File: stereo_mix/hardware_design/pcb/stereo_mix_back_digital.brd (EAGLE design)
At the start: 70 x 100 mm, 236 parts, among them IC1 LD117AS50TR, J1 WQP-PJ301M-12_JACK, J10 WQP-PJ301M-12_JACK, J11 WQP-PJ301M-12_JACK, J12 WQP-PJ301M-12_JACK, J13 WQP-PJ301M-12_JACK, J14 WQP-PJ301M-12_JACK, J15 WQP-PJ301M-12_JACK, J16 WQP-PJ301M-12_JACK, J17 WQP-PJ301M-12_JACK, J18 WQP-PJ301M-12_JACK, J2 WQP-PJ301M-12_JACK, J3 WQP-PJ301M-12_JACK, J4 WQP-PJ301M-12_JACK, J5 WQP-PJ301M-12_JACK, J6 WQP-PJ301M-12_JACK, J7 WQP-PJ301M-12_JACK, J8 WQP-PJ301M-12_JACK, J9 WQP-PJ301M-12_JACK, U1 TL072AD, U10 TL072AD, U11 MCP6002E/SN, U12 MCP6002E/SN, U13 MCP6002E/SN, U14 MCP6002E/SN, U15 MCP4922E/SL, U16 MCP4922E/SL, U17 TL072AD, U18 TL072AD, U19 MCP4822E-SN, U2 MCP6002E/SN, U20 MCP4822E-SN, U21 TL072AD, U22 TL072AD, U23 ATMEGA328P-AU, U24 MCP4822E-SN, U25 MCP4822E-SN, U26 TL072AD, U27 TL072AD, U28 TL072AD, U3 MCP6002E/SN, U4 MCP6002E/SN, U5 MCP6002E/SN, U6 MCP4922E/SL, U7 MCP4922E/SL, U8 TL072AD, U9 TL072AD

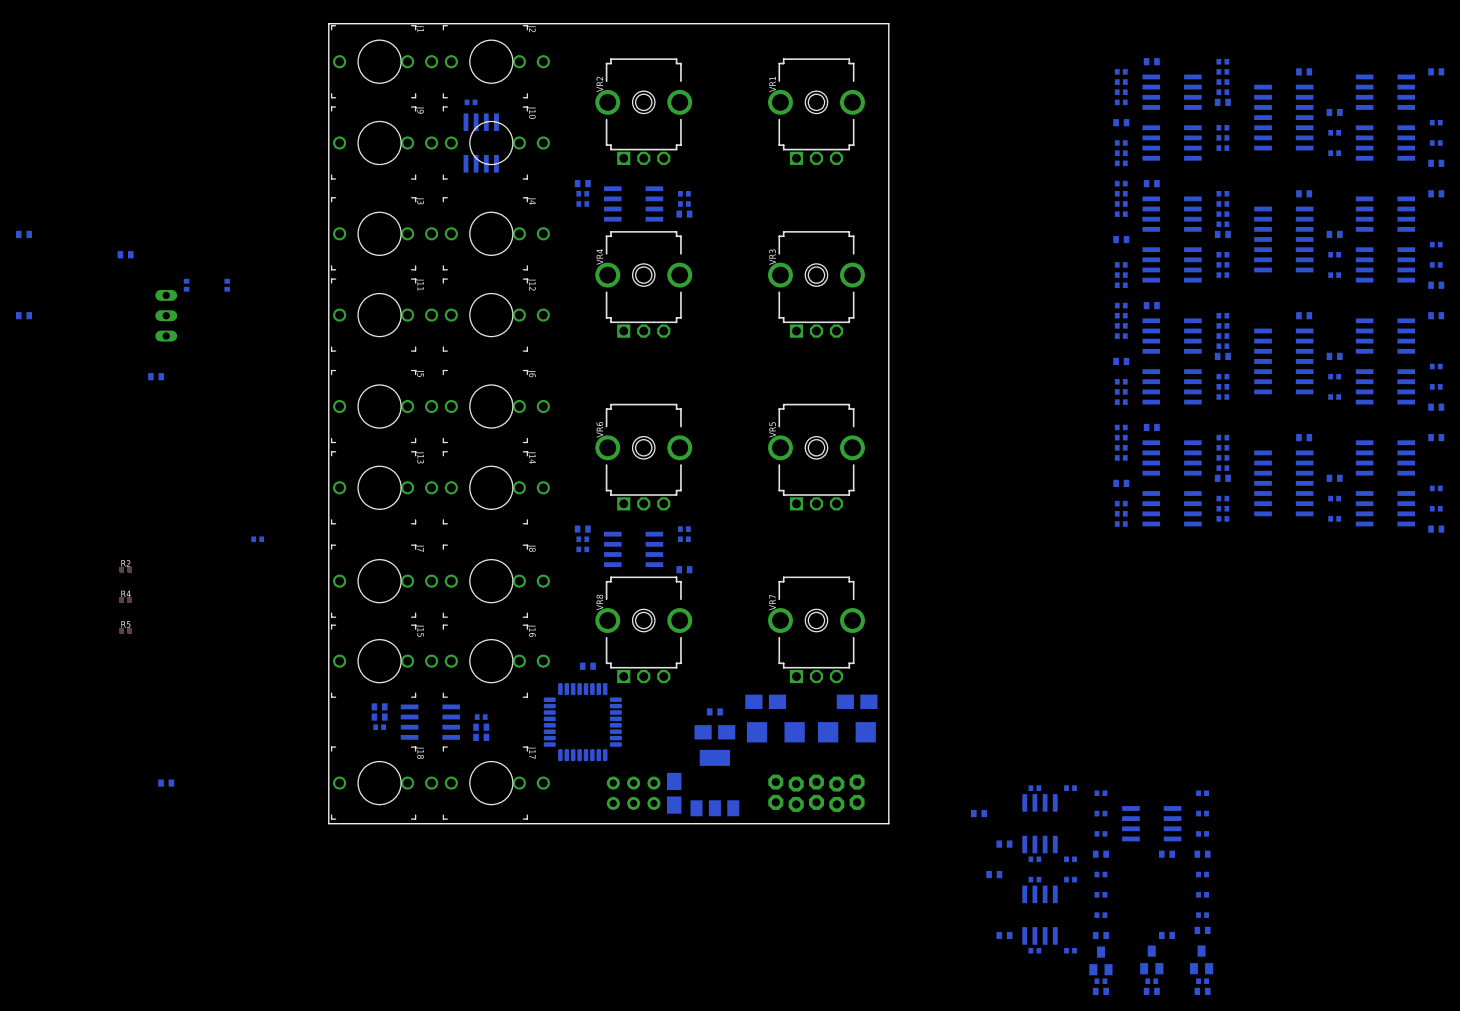
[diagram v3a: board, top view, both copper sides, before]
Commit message: Add new hardware revision of stereo mix
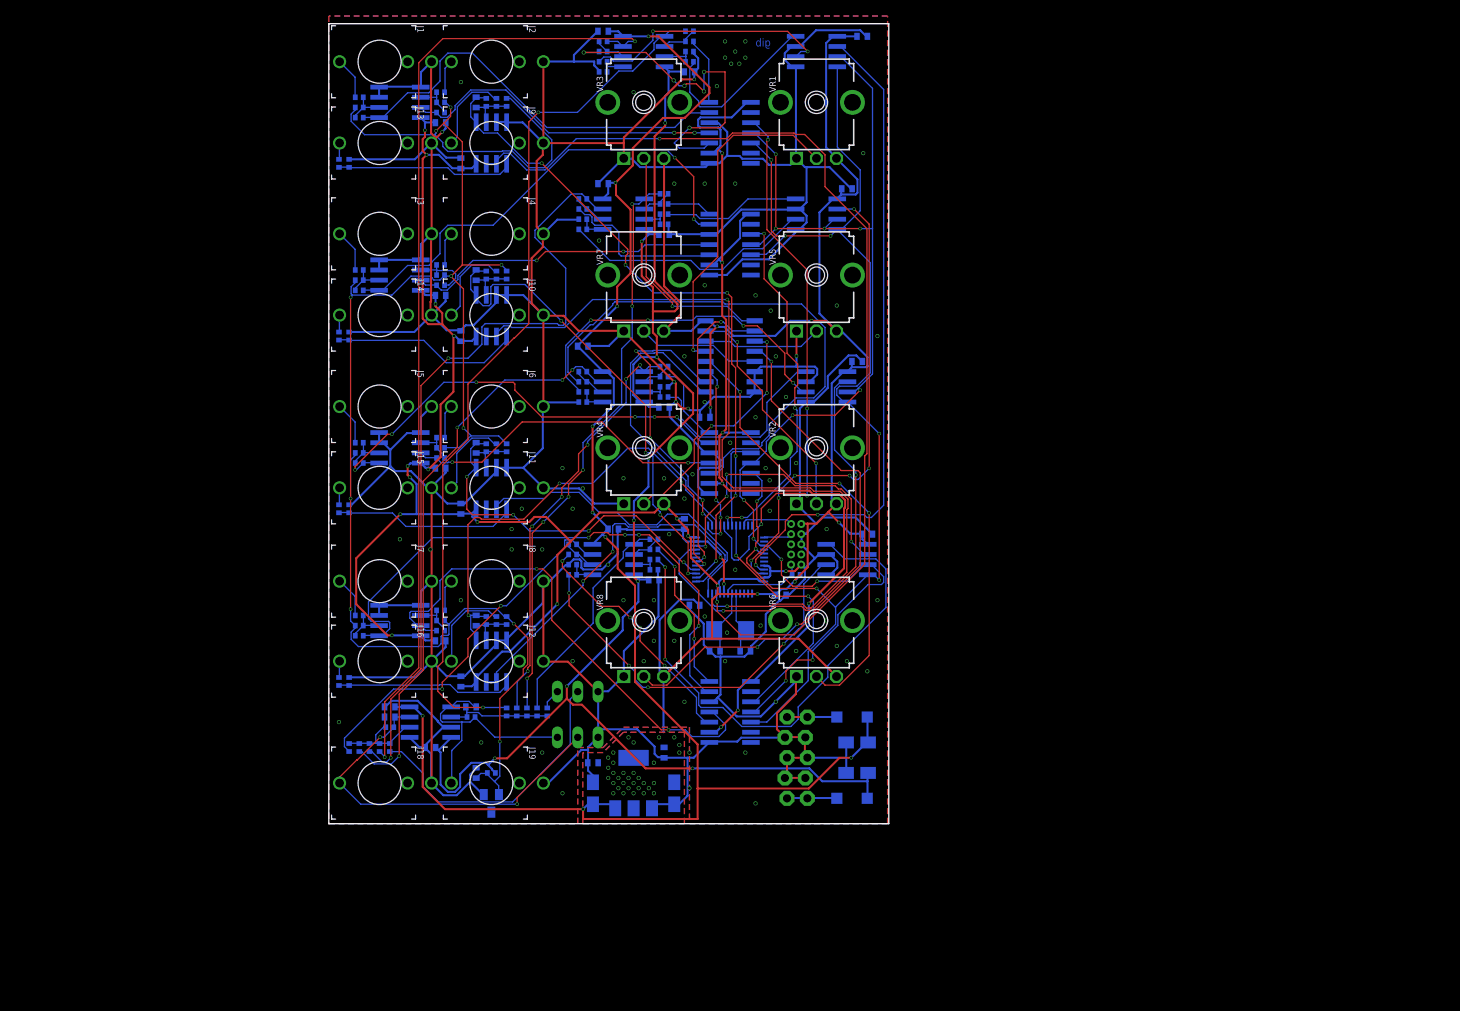
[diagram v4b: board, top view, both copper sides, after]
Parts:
- removed C45, C46, C47, C50, C51, C52, C53, C54, C58, C61, C62, C63: 100nF, jhbruhn-cr:C0402
- removed C48, C49: 6.8pF, jhbruhn-cr:C0402
- removed C55: EURO_POWER_LOCKFAT-LOCK, MusicThingModular:EURO_PWR_HEADER_LOCK
- removed C56, C57, C59, C60: 47uF, rcl:A/3216-18W
- removed D4, D5: LM4040AIM3-10.0, jhbruhn-ref:SOT23
- removed ISP1: AVRISP-6, adafruit:AVRISP
- removed JP3: (no value), jumper:JP2
- removed R100, R105, R106, R107, R108, R110, R111, R112, R113, R114, R91, R92, R97, R98, R99: 100k, jhbruhn-cr:R0402
- removed R101, R102, R103, R104, R93, R94, R95, R96: 43k, jhbruhn-cr:R0402
- removed R109: 10k, jhbruhn-cr:R0402
- removed R122, R123, R124: 470R, jhbruhn-cr:R0402
- removed U23: ATMEGA328P-AU, jhbruhn-mcu:TQFP-32
- removed U24, U25: MCP4822E-SN, jhbruhn-dac:SOIC8
- removed U26, U27, U28: TL072AD, jhbruhn-opamp:SOIC8
- added IC2: AMS1117-3.3, jhbruhn-ic:SOT223
- added J19: WQP-PJ301M-12_JACK, jhbruhn-physical:WQP-PJ301M-12_JACK
- added JP1, JP2: (no value), jumper:JP2
- added R44: 15k, jhbruhn-cr:R0402
- added R46, R49, R50: 47k, jhbruhn-cr:R0402
- added R6: 100k, jhbruhn-cr:R0402
- added X1: 8MHz, jhbruhn-cdr:NX5032
- C11, C12: value 4.7nF -> 100nF
- C21, C22: value 100nF -> 4.7nF
- C26, C27: value 100nF -> 22pF
- C32, C33: value 100nF -> 6.8pF
- C36: value 100nF -> EURO_POWER_LOCKFAT-LOCK; device jhbruhn-cr:C0402 -> MusicThingModular:EURO_PWR_HEADER_LOCK
- C37, C38, C39, C41: value 100nF -> 10uF; device jhbruhn-cr:C0402 -> jhbruhn-cdr:A/3216-18R
- D1, D2: value 1N4001 -> 1N4148W; device adafruit:SMADIODE -> jhbruhn-cdr:SOD123
- D3: value LM4040AIM3-5.0 -> LM4040AIM3-10.0
- IC1: value LD117AS50TR -> 4051D; device v-reg:SOT223 -> jhbruhn-ic:SO16
- J17: value WQP-PJ301M-12_JACK -> CORTEX_DEBUG_PTH; device jhbruhn-physical:WQP-PJ301M-12_JACK -> jhbruhn-physical:2X5-PTH-1.27MM
- R1, R3, R33, R37, R39, R5, R7: value 100k -> 91k
- R10, R11, R12, R41, R42, R43, R9: value 100k -> 15k
- R13, R14, R15, R16, R45, R47, R48, R51, R52: value 100k -> 47k
- R17, R18, R19, R20: value 24k -> 47k
- R21: value 200k -> 100k
- R23: value 200k -> 300k
- R25, R28, R57, R58, R59, R60: value 100k -> 300k
- R26: value 51k -> 300k
- R27: value 51k -> 100k
- R30, R31, R34, R66, R68, R82, R83: value 24k -> 100k
- R35: value 24k -> 91k
- R65, R67, R78, R79: value 24k -> 200k
- R73, R74: value 51k -> 33k
- R75, R76: value 100k -> 33k
- R77, R80: value 100k -> 200k
- R85: value 100k -> 10k
- R90: value 100k -> 470R
- U1, U10, U9: value TL072AD -> MCP4822E-SN; device jhbruhn-opamp:SOIC8 -> jhbruhn-dac:SOIC8
- U11, U12, U3, U4: value MCP6002E/SN -> MCP6002T-I/SN
- U13, U14, U5: value MCP6002E/SN -> MCP4922E/SL; device jhbruhn-opamp:SOIC8 -> jhbruhn-dac:SO-14
- U15, U16, U7: value MCP4922E/SL -> TL072CD; device jhbruhn-dac:SO-14 -> jhbruhn-opamp:SOIC8
- U17, U18: value TL072AD -> MCP6002T-I/SN
- U19, U20: value MCP4822E-SN -> MCP6002T-I/SN; device jhbruhn-dac:SOIC8 -> jhbruhn-opamp:SOIC8
- U2: value MCP6002E/SN -> MCP4822E-SN; device jhbruhn-opamp:SOIC8 -> jhbruhn-dac:SOIC8
- U21: value TL072AD -> STM32F030C8T6; device jhbruhn-opamp:SOIC8 -> jhbruhn-mcu:LQFP48
- U22, U8: value TL072AD -> TL072CD
- moved C35 153.0 mm to (7.62, 14.6), turned to 0 degrees
- moved C40 142.2 mm to (18.4, 6.35), turned to 90 degrees
- moved R30 133.5 mm to (6.35, 9.53), turned to 90 degrees
- moved U22 132.4 mm to (12.7, 12.7)
- moved R38 127.6 mm to (3.81, 26.0)
- moved U20 125.0 mm to (20.3, 20.3), turned to 180 degrees
- moved R32 124.7 mm to (5.08, 9.53), turned to 90 degrees
- moved R23 123.4 mm to (45.1, 99.1)
- moved R24 123.4 mm to (45.1, 96.5), turned to 180 degrees
- moved C39 123.1 mm to (33.0, 3.81), turned to 90 degrees
- moved U19 122.2 mm to (20.3, 41.9), turned to 180 degrees
- moved C19 122.2 mm to (18.4, 90.2), turned to 90 degrees
- moved R73 119.4 mm to (19.7, 90.2), turned to 90 degrees
- moved R29 119.2 mm to (22.2, 14.0), turned to 270 degrees
- moved R21 118.1 mm to (34.3, 94.0)
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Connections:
- removed net 1_PAN_CV_IN: J10.P$1_TIP, R114.1
- removed net 1_VOLUME_CV: J9.P$1_TIP, R25.2
- removed net N$12: U1.3, VR2.2
- removed net N$13: R22.1, R7.2, U1.1
- removed net N$18: R1.2, R7.1, U1.2
- removed net N$43: U1.5, VR4.2
- removed net N$45: U10.5, VR8.2
- removed net N$56: R24.1, R8.2, U1.7
- removed net N$57: R3.2, R8.1, U1.6
- removed net N$58: C34.1, U23.20
- removed net N$60: R53.2, R70.1, U10.1
- removed net N$61: R43.2, R53.1, U10.2
- removed net N$64: R54.2, R72.1, U10.7
- removed net N$65: R45.2, R54.1, U10.6
- removed net N$74: R93.2, R97.1, U21.2
- removed net N$77: R100.1, R96.2, U22.6
- removed net N$78: R101.2, R105.1, U26.2
- removed net N$79: R102.2, R106.1, U26.6
- removed net N$80: R103.2, R107.1, U27.2
- removed net N$81: R104.2, R108.1, U27.6
- removed net N$83: U10.3, VR6.2
- removed net REF_10: C61.1, D4.1, R123.1
- removed net REF_5: C58.1, D3.1, R1.1, R122.1, R3.1, R43.1, R45.1, VR2.3, VR4.3, VR6.3, VR8.3
- removed net RESET: ISP1.5, R109.1, U23.29
- new net +3V3: C10.1, C11.1, C12.1, C13.1, C14.1, C15.1, C16.1, C17.1, C18.1, C23.1, C24.1, C25.1, C28.1, C29.1, C30.1, C31.1, C41.+, C42.1, C9.1, IC1.16, IC2.4, J17.1, R85.2, U1.1, U10.1, U11.8, U12.8, U17.8, U18.8, U19.8, U2.1, U20.8, U21.1, U21.24, U21.48, U21.9, U3.8, U4.8, U9.1, VR1.3, VR2.3, VR3.3, VR4.3, VR5.3, VR6.3, VR7.3, VR8.3
- new net MUX_ADDR_0: IC1.11, U21.25
- new net MUX_ADDR_1: IC1.10, U21.26
- new net MUX_ADDR_2: IC1.9, U21.27
- new net N$84: J9.P$1_TIP, R66.1
- new net N$89: J13.P$1_TIP, R77.2
- new net NRST: J17.10, R85.1, U21.7
- new net PAN_1_POT: IC1.1, VR3.2
- new net PAN_2_POT: IC1.5, VR7.2
- new net PAN_3_POT: IC1.2, VR4.2
- new net PAN_4_POT: IC1.4, VR8.2
- new net POT_MUX: IC1.3, U21.18
- new net SWDCLK: J17.4, U21.37
- new net SWDIO: J17.2, U21.34
- new net VOL_1_POT: IC1.13, VR1.2
- new net VOL_2_POT: IC1.14, VR5.2
- new net VOL_3_POT: IC1.15, VR2.2
- new net VOL_4_POT: IC1.12, VR6.2
- net +12V: now also C35.1, C37.+, C39.+, IC2.3, U15.8, U16.8, U7.8; no longer C13.1, C41.1, C42.1, C45.1, C46.1, C52.1, C53.1, C54.1, C56.+, C59.+, C9.1, IC1.3, R122.2, R123.2, U1.8, U10.8, U17.8, U18.8, U21.8, U26.8, U27.8, U28.8, U9.8
- net +5V: now also U13.1, U13.9, U14.1, U14.9, U5.1, U5.9; no longer C15.1, C16.1, C17.1, C18.1, C21.1, C22.1, C23.1, C24.1, C25.1, C26.1, C27.1, C28.1, C29.1, C30.1, C31.1, C32.1, C33.1, C35.1, C36.1, C60.+, C62.1, IC1.4, ISP1.2, R109.2, U11.8, U12.8, U13.8, U14.8, U15.1, U15.9, U16.1, U16.9, U19.1, U2.8, U20.1, U23.18, U23.4, U23.6, U24.1, U25.1, U3.8, U4.8, U5.8, U7.1, U7.9
- net -12V: now also C34.2, C38.-, R90.2, U15.4, U16.4, U7.4; no longer C10.2, C14.2, C37.2, C38.2, C39.2, C40.2, C47.2, C50.2, C51.2, C57.-, R124.2, U1.4, U10.4, U17.4, U18.4, U21.4, U26.4, U27.4, U28.4, U9.4
- net 1_IN_L: now also R2.1; no longer R10.1
- net 1_IN_R: now also R4.1; no longer R12.1
- net 2_IN_L: now also R6.1; no longer R14.1
- net 2_IN_R: now also R8.1; no longer R16.1
- net 2_PAN_CV_IN: now also J10.P$1_TIP, R68.1; no longer J12.P$1_TIP, R2.1
- net 2_VOLUME_CV: now also J14.P$1_TIP, R78.2; no longer J11.P$1_TIP, R37.2
- net 3_IN_L: now also R34.1; no longer R56.1
- net 3_IN_R: now also R36.1; no longer R58.1
- net 3_PAN_CV_IN: now also J11.P$1_TIP, R70.1; no longer J14.P$1_TIP, R4.1
- net 3_VOLUME_CV: now also J15.P$1_TIP, R79.2; no longer J13.P$1_TIP, R63.2
- net 4_IN_L: now also R38.1; no longer R60.1
- net 4_IN_R: now also R40.1; no longer R62.1
- net 4_PAN_CV_IN: now also J12.P$1_TIP, R72.1; no longer J16.P$1_TIP, R5.1
- net 4_VOLUME_CV: now also J16.P$1_TIP, R80.2; no longer J15.P$1_TIP, R75.2
- net AREF_-10: now also C40.1, D3.2, R1.1, R3.1, R33.1, R35.1, R37.1, R39.1, R5.1, R65.1, R67.1, R7.1, R90.1; no longer C63.1, D5.2, R11.1, R124.1, R13.1, R15.1, R21.1, R23.1, R55.1, R57.1, R59.1, R61.1, R9.1
- net AUX_IN_L: now also JP1.1, R86.1; no longer JP3.1, R110.1
- net AUX_IN_R: now also JP1.2, R87.1; no longer JP3.2, R111.1
- net BIAS_DAC1_L: now also R16.1, U1.8; no longer R29.1, R97.2, U21.1
- net BIAS_DAC1_R: now also R15.1, U1.6; no longer R32.1, R98.2, U21.7
- net BIAS_DAC2_L: now also R20.1, U2.8; no longer R33.1, R99.2, U22.1
- net BIAS_DAC2_R: now also R19.1, U2.6; no longer R100.2, R36.1, U22.7
- net BIAS_DAC3_L: now also R51.1, U9.8; no longer R105.2, R77.1, U26.1
- net BIAS_DAC3_R: now also R47.1, U9.6; no longer R106.2, R80.1, U26.7
- net BIAS_DAC4_L: now also R52.1, U10.8; no longer R107.2, R81.1, U27.1
- net BIAS_DAC4_R: now also R50.1, U10.6; no longer R108.2, R84.1, U27.7
- net CS_BIAS_DAC_1: now also U1.2, U21.45; no longer U19.2, U23.2
- net CS_BIAS_DAC_2: now also U2.2, U21.46; no longer U20.2, U23.9
- net CS_BIAS_DAC_3: now also U21.21, U9.2; no longer U23.10, U24.2
- net CS_BIAS_DAC_4: now also U10.2, U21.22; no longer U23.11, U25.2
- net CS_DAC_1: now also U21.29, U5.3; no longer U23.30, U6.3
- net CS_DAC_2: now also U21.30, U6.3; no longer U23.31, U7.3
- net CS_DAC_3: now also U13.3, U21.31; no longer U15.3, U23.32
- net CS_DAC_4: now also U14.3, U21.32; no longer U16.3, U23.1
- net GND: now also C10.2, C11.2, C12.2, C14.2, C26.1, C27.1, C34.1, C36.GND1, C36.GND2, C36.GND3, C36.GND4, C36.GND5, C36.GND6, C37.-, C38.+, C39.-, C40.2, C41.-, D3.1, IC1.6, IC1.7, IC1.8, IC2.1, J1.P$3_SLEEVE, J10.P$3_SLEEVE, J11.P$3_SLEEVE, J12.P$3_SLEEVE, J13.P$3_SLEEVE, J14.P$3_SLEEVE, J15.P$3_SLEEVE, J16.P$3_SLEEVE, J17.3, J17.5, J17.9, J18.P$3_SLEEVE, J19.P$3_SLEEVE, J2.P$3_SLEEVE, J3.P$3_SLEEVE, J4.P$3_SLEEVE, J5.P$3_SLEEVE, J6.P$3_SLEEVE, J7.P$3_SLEEVE, J8.P$3_SLEEVE, J9.P$3_SLEEVE, JP1.3, JP2.3, R21.1, R22.2, R24.2, R27.2, R53.1, R54.1, R55.1, R56.1, R81.1, R82.1, R83.1, R84.1, U1.5, U1.7, U10.5, U10.7, U13.12, U13.8, U14.12, U14.8, U17.4, U18.4, U19.3, U19.4, U2.7, U20.3, U20.4, U21.23, U21.44, U21.47, U21.8, U4.5, U5.12, U5.8, U9.7, VR1.1, VR3.1, VR5.1, VR7.1; no longer C10.1, C14.1, C21.2, C22.2, C26.2, C27.2, C32.2, C33.2, C34.2, C36.2, C37.1, C38.1, C39.1, C40.1, C41.2, C45.2, C46.2, C47.1, C50.1, C51.1, C52.2, C53.2, C54.2, C55.GND1, C55.GND2, C55.GND3, C55.GND4, C55.GND5, C55.GND6, C56.-, C57.+, C58.2, C59.-, C60.-, C61.2, C62.2, C63.2, D3.2, D4.2, D5.1, IC1.1, ISP1.6, JP3.3, R28.1, R40.1, R64.1, R76.1, U13.3, U13.4, U14.3, U14.4, U15.12, U15.8, U16.12, U16.8, U17.5, U18.5, U19.5, U19.7, U2.3, U2.4, U20.5, U20.7, U21.3, U21.5, U23.21, U23.3, U23.5, U24.5, U24.7, U25.5, U25.7, U26.3, U26.5, U27.3, U27.5, U28.3, U28.5, U5.3, U5.4, U7.12, U7.8, U8.3, U8.5, U9.3
- net MISO: now also U21.40; no longer ISP1.1, U23.16
- net MOSI: now also U1.4, U10.4, U13.5, U14.5, U2.4, U21.41, U5.5, U9.4; no longer ISP1.4, U15.5, U16.5, U19.4, U20.4, U23.15, U24.4, U25.4, U7.5
- net N$1: now also R13.1, U5.14; no longer R30.1, U6.14
- net N$10: now also R14.1, U5.10; no longer R31.1, U6.10
- net N$11: now also C20.1, R67.2, R68.2, R74.1, U18.2; no longer C12.1, R2.2, R23.2, R24.2, R27.1, U5.2
- net N$14: now also R16.2, R24.1, U7.3; no longer R93.1, U19.8
- net N$15: now also R77.1, R81.2, U17.5; no longer R25.1, R28.2, U4.5
- net N$16: now also R15.2, R21.2, U7.5; no longer R94.1, U19.6
- net N$17: now also R78.1, R82.2, U18.5; no longer R37.1, R40.2, U5.5
- net N$19: now also R12.1, R7.2, R8.2, U4.6; no longer R15.2, R16.2, R20.1, U3.6
- net N$2: now also R10.1, R3.2, R4.2, U3.6; no longer R11.2, R12.2, R18.1, U2.6
- net N$20: now also R12.2, U4.7, U6.11; no longer R20.2, U3.7, U7.11
- net N$21: now also R11.2, U4.1, U6.13; no longer R19.2, U3.1, U7.13
- net N$22: now also R11.1, R5.2, R6.2, U4.2; no longer R13.2, R14.2, R19.1, U3.2
- net N$23: now also R17.1, U6.14; no longer R34.1, U7.14
- net N$24: now also R17.2, R26.1, U8.2; no longer R33.2, R34.2, R39.1, U9.2
- net N$25: now also R26.2, R31.1, U8.1; no longer R39.2, R48.1, U9.1
- net N$26: now also R18.2, R28.1, U8.6; no longer R35.2, R36.2, R42.1, U9.6
- net N$27: now also R18.1, U6.10; no longer R35.1, U7.10
- net N$28: now also R28.2, R32.1, U8.7; no longer R42.2, R52.1, U9.7
- net N$29: now also R35.2, R36.2, R42.1; no longer R57.2, R58.2, R66.1
- net N$3: now also R13.2, R23.1, U7.2; no longer R29.2, R30.2, R38.1, U8.2
- net N$30: now also R42.2, U13.11; no longer R66.2, U15.11
- net N$31: now also R41.2, U13.13; no longer R65.2, U15.13
- net N$32: now also C19.1, R65.2, R66.2, R73.1, U17.2; no longer C11.1, R114.2, R21.2, R22.2, R26.1, U4.2
- net N$33: now also R33.2, R34.2, R41.1; no longer R55.2, R56.2, R65.1
- net N$34: now also R45.1, U13.14; no longer R78.1, U15.14
- net N$35: now also R45.2, R57.1, U15.2; no longer R77.2, R78.2, R85.1, U17.2
- net N$36: now also R57.2, R61.1, U15.1; no longer R85.2, R89.1, U17.1
- net N$37: now also R46.2, R59.1, U15.6; no longer R79.2, R80.2, R87.1, U17.6
- net N$38: now also R46.1, U13.10; no longer R79.1, U15.10
- net N$39: now also R59.2, R63.1, U15.7; no longer R87.2, R91.1, U17.7
- net N$4: now also R9.2, U3.1, U5.13; no longer R17.2, U2.1, U6.13
- net N$40: now also R39.2, R40.2, R44.1; no longer R61.2, R62.2, R68.1
- net N$41: now also R44.2, U14.11; no longer R68.2, U16.11
- net N$44: now also R43.2, U14.13; no longer R67.2, U16.13
- net N$46: now also R37.2, R38.2, R43.1; no longer R59.2, R60.2, R67.1
- net N$47: now also C36.POS1, C36.POS2; no longer C55.POS1, C55.POS2
- net N$48: now also C36.NEG1, C36.NEG2; no longer C55.NEG1, C55.NEG2
- net N$49: now also R48.1, U14.14; no longer R82.1, U16.14
- net N$5: now also R10.2, U3.7, U5.11; no longer R18.2, U2.7, U6.11
- net N$50: now also R48.2, R58.1, U16.2; no longer R81.2, R82.2, R86.1, U18.2
- net N$51: now also R58.2, R62.1, U16.1; no longer R86.2, R90.1, U18.1
- net N$52: now also R49.2, R60.1, U16.6; no longer R83.2, R84.2, R88.1, U18.6
- net N$53: now also R49.1, U14.10; no longer R83.1, U16.10
- net N$54: now also R60.2, R64.1, U16.7; no longer R88.2, R92.1, U18.7
- net N$55: now also C22.1, R76.1, U20.2; no longer C20.1, R5.2, R74.1, U13.2
- net N$59: now also C21.1, R75.1, U19.2; no longer C19.1, R4.2, R73.1, U14.2
- net N$6: now also R1.2, R2.2, R9.1, U3.2; no longer R10.2, R17.1, R9.2, U2.2
- net N$66: now also R79.1, R83.2, U19.5; no longer R63.1, R64.2, U14.5
- net N$67: now also R20.2, R27.1, U8.3; no longer R95.1, U20.8
- net N$68: now also R19.2, R22.1, U8.5; no longer R96.1, U20.6
- net N$69: now also R80.1, R84.2, U20.5; no longer R75.1, R76.2, U13.5
- net N$7: now also R25.2, R30.1, U7.7; no longer R41.2, R51.1, U8.7
- net N$70: now also R51.2, R53.2, U15.3; no longer R101.1, U24.8
- net N$71: now also R47.2, R54.2, U15.5; no longer R102.1, U24.6
- net N$72: now also R50.2, R56.2, U16.5; no longer R103.1, U25.8
- net N$73: now also R52.2, R55.2, U16.3; no longer R104.1, U25.6
- net N$75: now also C27.2, X1.P$1; no longer R94.2, R98.1
- net N$76: now also C26.2, U21.5, X1.P$2; no longer R95.2, R99.1, U22.2
- net N$8: now also R23.2, R29.1, U7.1; no longer R38.2, R47.1, U8.1
- net N$9: now also R14.2, R25.1, U7.6; no longer R31.2, R32.2, R41.1, U8.6
- net OUT_L: now also C32.2, J19.P$1_TIP, JP2.1, R88.2, U22.1; no longer C48.2, J17.P$1_TIP, R112.2, U28.1
- net OUT_R: now also C33.2, JP2.2, R89.2, U22.7; no longer C49.2, R113.2, U28.7
- net PAN_CV_1: now also C19.2, R73.2, U17.1, U21.14; no longer C11.2, R26.2, U23.27, U4.1
- net PAN_CV_2: now also C20.2, R74.2, U18.1, U21.15; no longer C12.2, R27.2, U23.28, U5.1
- net PAN_CV_3: now also C21.2, R75.2, U19.1, U21.16; no longer C19.2, R73.2, U14.1, U23.19
- net PAN_CV_4: now also C22.2, R76.2, U20.1, U21.17; no longer C20.2, R74.2, U13.1, U23.22
- net SCK: now also U1.3, U10.3, U13.4, U14.4, U2.3, U21.39, U5.4, U9.3; no longer ISP1.3, U15.4, U16.4, U19.3, U20.3, U23.17, U24.3, U25.3, U7.4
- net SUM_L: now also C32.1, R29.2, R31.2, R61.2, R62.2, R86.2, R88.1, U22.2; no longer C48.1, R110.2, R112.1, R47.2, R48.2, R89.2, R90.2, U28.2
- net SUM_R: now also C33.1, R30.2, R32.2, R63.2, R64.2, R87.2, R89.1, U22.6; no longer C49.1, R111.2, R113.1, R51.2, R52.2, R91.2, R92.2, U28.6
- net VOL_CV_1: now also U17.6, U17.7, U21.10; no longer U23.23, U4.6, U4.7
- net VOL_CV_2: now also U18.6, U18.7, U21.11; no longer U23.24, U5.6, U5.7
- net VOL_CV_3: now also U19.6, U19.7, U21.12; no longer U14.6, U14.7, U23.25
- net VOL_CV_4: now also U20.6, U20.7, U21.13; no longer U13.6, U13.7, U23.26
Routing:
- net GND: track 0.00 -> 841.0 mm, vias 0 -> 83
- net +3V3: track 0.00 -> 407.7 mm, vias 0 -> 52
- net AREF_-10: track 0.00 -> 220.4 mm, vias 0 -> 10
- net +12V: track 0.00 -> 212.2 mm, vias 0 -> 9
- net -12V: track 0.00 -> 196.8 mm, vias 0 -> 9
- net MOSI: track 0.00 -> 155.6 mm, vias 0 -> 8
- net SCK: track 0.00 -> 154.7 mm, vias 0 -> 12
- net VOL_CV_1: track 0.00 -> 126.1 mm, vias 0 -> 2
- net +5V: track 0.00 -> 125.9 mm, vias 0 -> 7
- net N$7: track 0.00 -> 122.0 mm, vias 0 -> 2
- net N$8: track 0.00 -> 110.2 mm, vias 0 -> 2
- net VOL_CV_2: track 0.00 -> 101.5 mm, vias 0 -> 2
- net N$28: track 0.00 -> 98.6 mm, vias 0 -> 2
- net PAN_CV_1: track 0.00 -> 85.4 mm, vias 0 -> 6
- net CS_BIAS_DAC_1: track 0.00 -> 81.7 mm, vias 0 -> 2
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- added copper zone on layer 1, net +3V3
- added copper zone on layer 16, net +3V3
- added copper zone on layer 1, net GND
- added copper zone on layer 16, net GND
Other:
- board text added: "gib"
- board text added: "jhbruhn 2020"
- board text added: "stereo_mix v3"
- board text removed: "jhbruhn 2019 stereo mix back digital v1.1"

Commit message: Update jlcpcb-eagle
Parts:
- added SW1, SW2, SW3, SW4: (no value), jhbruhn-physical:PB6149L
- C37, C38, C39, C41: device jhbruhn-cdr:A/3216-18R -> jhbruhn-cdr:CASE-A_3216
- D1, D2: value 1N4148W -> SS54; device jhbruhn-cdr:SOD123 -> jhbruhn-cdr:SMA
- moved C25 3.59 mm to (39.4, 11.4), turned to 90 degrees
- moved C39 1.27 mm to (31.8, 3.81), turned to 270 degrees
- moved D1 1.27 mm to (65.4, 14.6), turned to 0 degrees
- moved C42 0.95 mm to (34.0, 7.62)
- moved D2 0.63 mm to (65.4, 2.54), turned to 180 degrees
- turned C37 to 180 degrees
- turned C38 to 0 degrees
- turned C41 to 90 degrees
- turned U21 to 0 degrees
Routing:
- net +3V3: track 407.7 -> 415.5 mm
- net GND: track 841.0 -> 835.6 mm
- net +12V: track 212.2 -> 217.2 mm
- net -12V: track 196.8 -> 200.0 mm

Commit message: stereo mix routing nearly finished
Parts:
- added C43, C44, C45, C46, C57, C58, C59, C60, C61, C62, C63, C64: 100nF, jhbruhn-cr:C0402
- added C47, C48: 22uF, jhbruhn-cdr:C0805
- added C49, C50, C51, C52, C53, C54, C55, C56: 10uF, jhbruhn-cr:C0402
- added R91, R92, R93, R94: 100R, jhbruhn-cdr:R0402
- C32, C33: value 6.8pF -> 220pF
- D1, D2: value SS54 -> B5819W; device jhbruhn-cdr:SMA -> jhbruhn-cdr:SOD123
- IC1: value 4051D -> 4051CD4051; device jhbruhn-ic:SO16 -> jhbruhn-ic:SOIC16N
- moved JP1 50.8 mm to (-19.7, 15.2)
- moved JP2 50.8 mm to (-19.7, 9.53)
- moved C38 41.0 mm to (25.4, 1.27)
- moved D2 34.3 mm to (31.1, 2.86), turned to 0 degrees
- moved C28 30.9 mm to (42.2, 6.67), turned to 180 degrees
- moved IC1 28.5 mm to (63.2, 33.0)
- moved C29 27.3 mm to (32.4, 15.9), turned to 0 degrees
- moved J17 26.7 mm to (50.2, 9.53), turned to 180 degrees
- moved C39 26.7 mm to (58.4, 3.49), turned to 0 degrees
- moved U21 25.0 mm to (37.5, 11.4)
- moved C27 23.3 mm to (36.8, 1.27), turned to 0 degrees
- moved R85 23.3 mm to (54.0, 8.26), turned to 270 degrees
- moved X1 23.0 mm to (39.4, 3.81)
- moved C26 22.7 mm to (41.9, 1.27)
- moved R81 19.8 mm to (22.2, 85.1), turned to 90 degrees
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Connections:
- removed net +5V: U13.1, U13.9, U14.1, U14.9, U5.1, U5.9, U6.1, U6.9
- new net LED_1: R91.1, U21.43
- new net LED_2: R92.1, U21.28
- new net LED_3: R93.1, U21.2
- new net LED_4: R94.1, U21.3
- new net N$12: R91.2, SW1.A
- new net N$13: R92.2, SW2.A
- new net N$18: R93.2, SW3.A
- new net N$42: R94.2, SW4.A
- new net SWITCH_1: SW1.1, SW1.2, U21.33
- new net SWITCH_2: SW2.1, SW2.2, U21.19
- new net SWITCH_3: SW3.1, SW3.2, U21.20
- new net SWITCH_4: SW4.1, SW4.2, U21.42
- net +12V: now also C48.1
- net +3V3: now also C43.1, C44.1, C45.1, C46.1, C49.1, C50.1, C51.1, C52.1, C53.1, C54.1, C55.1, C56.1, U13.1, U13.9, U14.1, U14.9, U5.1, U5.9, U6.1, U6.9
- net -12V: now also C47.2
- net 1_IN_L: now also J2.P$2_SWITCH
- net 2_IN_L: now also J4.P$2_SWITCH
- net 3_IN_L: now also J6.P$2_SWITCH
- net 4_IN_L: now also J8.P$2_SWITCH
- net GND: now also C43.2, C44.2, C45.2, C46.2, C47.1, C48.2, C49.2, C50.2, C51.2, C52.2, C53.2, C54.2, C55.2, C56.2, C57.2, C58.2, C59.2, C60.2, C61.2, C62.2, C63.2, C64.2, SW1.3, SW1.4, SW1.K, SW2.3, SW2.4, SW2.K, SW3.3, SW3.4, SW3.K, SW4.3, SW4.4, SW4.K
- net OUT_L: now also J18.P$2_SWITCH
- net PAN_1_POT: now also C61.1
- net PAN_2_POT: now also C62.1
- net PAN_3_POT: now also C63.1
- net PAN_4_POT: now also C64.1
- net VOL_1_POT: now also C57.1
- net VOL_2_POT: now also C58.1
- net VOL_3_POT: now also C59.1
- net VOL_4_POT: now also C60.1
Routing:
- net GND: track 835.6 -> 112.8 mm, vias 83 -> 4
- net +3V3: track 415.5 -> 75.2 mm, vias 52 -> 2
- net +12V: track 217.2 -> 25.4 mm, vias 9 -> 0
- net -12V: track 200.0 -> 20.2 mm, vias 9 -> 0
- net +5V: track 125.9 -> 0.00 mm, vias 7 -> 0
- net LED_1: track 0.00 -> 83.2 mm, vias 0 -> 2
- net PAN_CV_1: track 85.4 -> 157.9 mm
- net BIAS_DAC4_L: track 66.3 -> 7.52 mm, vias 2 -> 0
- net PAN_2_POT: track 15.5 -> 72.1 mm, vias 0 -> 4
- net PAN_1_POT: track 31.0 -> 84.9 mm, vias 1 -> 2
- net LED_3: track 0.00 -> 52.1 mm, vias 0 -> 4
- net LED_2: track 0.00 -> 49.7 mm, vias 0 -> 2
- net CS_BIAS_DAC_1: track 81.7 -> 130.0 mm, vias 2 -> 8
- net CS_BIAS_DAC_2: track 61.0 -> 108.9 mm
- net PAN_CV_2: track 60.2 -> 104.2 mm, vias 4 -> 8
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- removed copper zone on layer 1, net +3V3
- removed copper zone on layer 16, net +3V3
- removed copper zone on layer 1, net GND
- removed copper zone on layer 16, net GND
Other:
- board text removed: "gib"

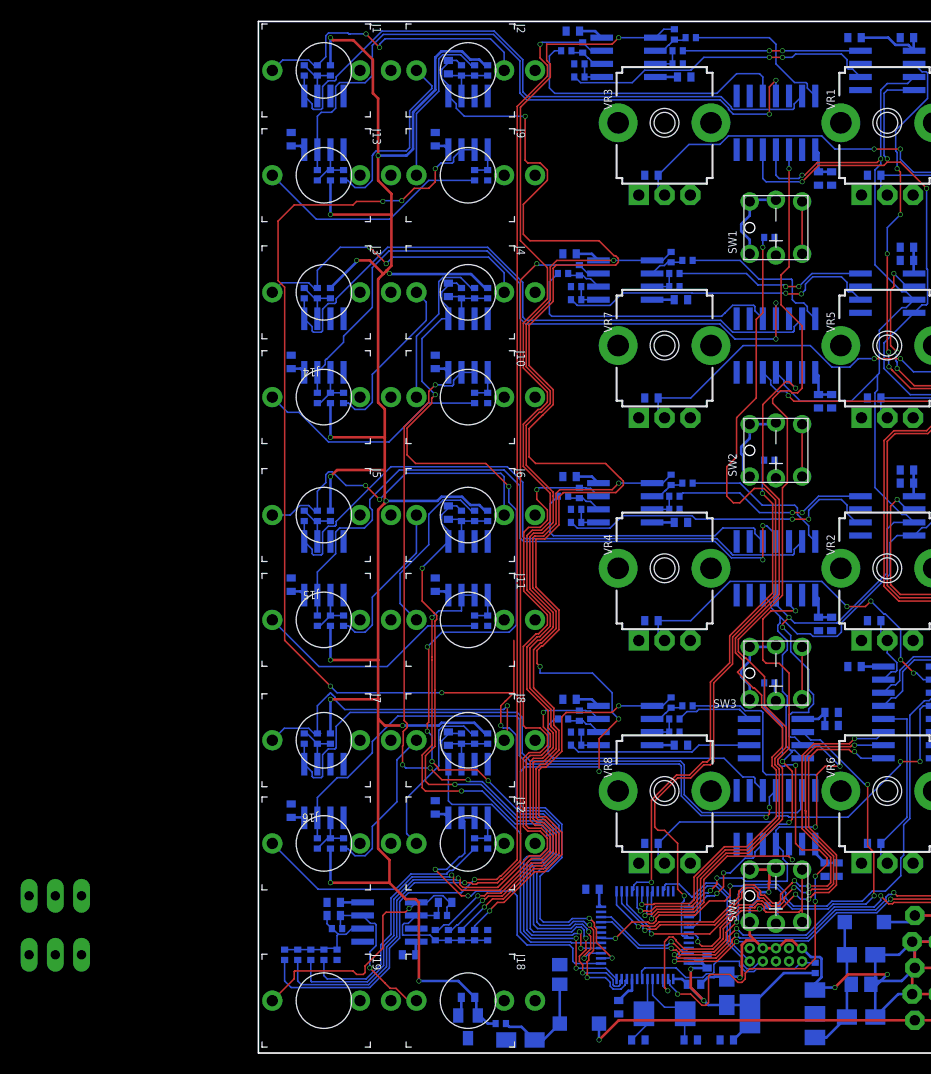
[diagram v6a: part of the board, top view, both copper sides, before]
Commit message: All very important signals routed
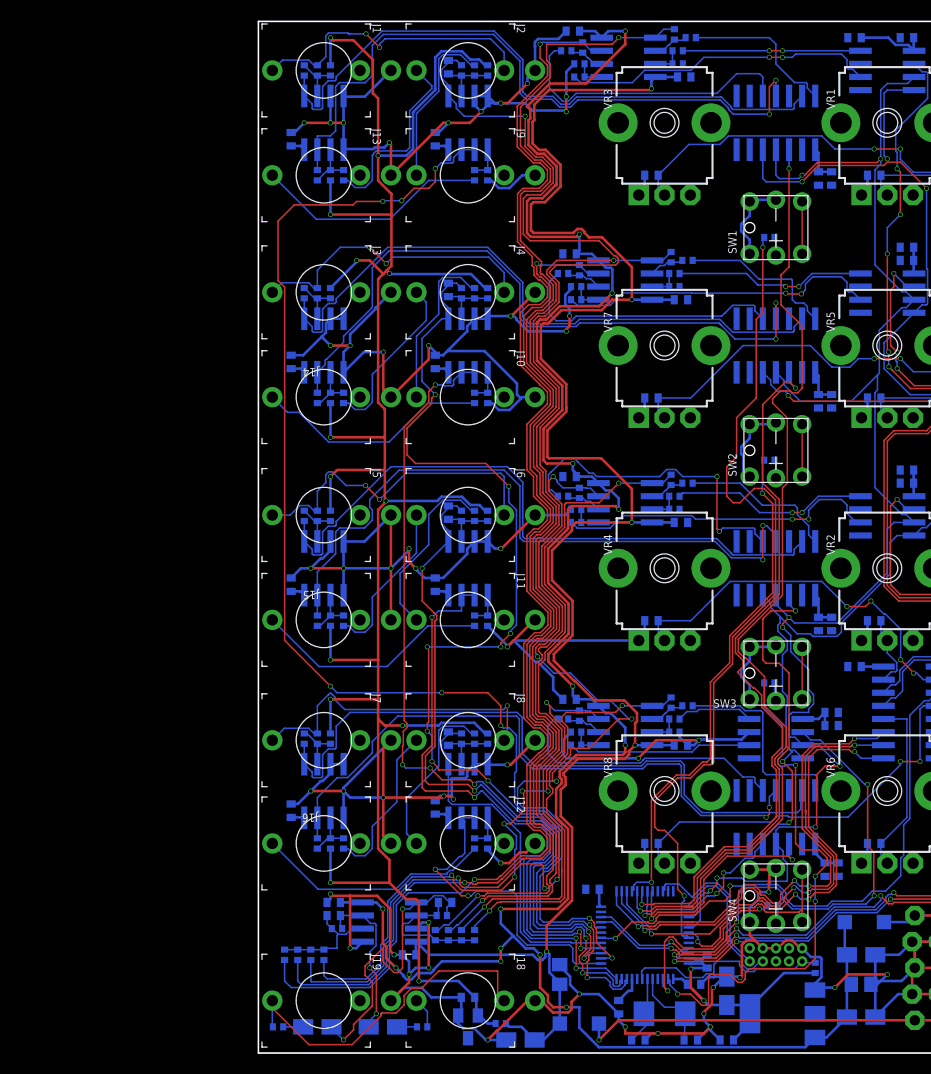
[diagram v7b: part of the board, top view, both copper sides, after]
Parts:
- removed JP1, JP2: (no value), jumper:JP2
- removed R86, R87: 100k, jhbruhn-cr:R0402
- added C65, C66: 10uF, jhbruhn-cdr:CASE-A_3216
- added R95, R96: 1k, jhbruhn-cdr:R0402
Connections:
- removed net AUX_IN_L: JP1.1, R86.1
- removed net AUX_IN_R: JP1.2, R87.1
- new net N$43: J18.P$2_SWITCH, J19.P$1_TIP, R95.2
- new net N$45: C65.-, R95.1
- new net N$56: J18.P$1_TIP, R96.2
- new net N$57: C66.-, R96.1
- net GND: no longer JP1.3, JP2.3
- net OUT_L: now also C65.+; no longer J18.P$2_SWITCH, J19.P$1_TIP, JP2.1
- net OUT_R: now also C66.+; no longer J18.P$1_TIP, JP2.2
- net SUM_L: no longer R86.2
- net SUM_R: no longer R87.2
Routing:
- net GND: track 112.8 -> 540.4 mm, vias 4 -> 50
- net +12V: track 25.4 -> 224.0 mm, vias 0 -> 14
- net -12V: track 20.2 -> 186.2 mm, vias 0 -> 5
- net N$43: track 0.00 -> 33.3 mm
- net N$7: track 120.1 -> 138.5 mm
- net N$28: track 96.9 -> 110.0 mm
- net PAN_CV_1: track 157.9 -> 146.1 mm
- net VOL_CV_1: track 137.5 -> 130.1 mm
- net N$38: track 25.7 -> 31.3 mm, vias 0 -> 2
- net N$8: track 119.6 -> 125.1 mm
- net N$39: track 84.9 -> 88.9 mm, vias 2 -> 4
- net OUT_L: track 26.3 -> 29.4 mm, vias 1 -> 2
- net N$56: track 0.00 -> 2.98 mm
- net N$51: track 38.9 -> 41.3 mm
- net N$57: track 0.00 -> 1.94 mm
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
